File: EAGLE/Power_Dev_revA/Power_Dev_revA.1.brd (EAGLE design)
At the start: 63.5 x 31.8 mm, 36 parts, among them J5 MICRO_USB_SMD, Q1 SI2301CDS-T1-GE3, Q2 SI2301CDS-T1-GE3, U1 CN3791, U3 DW01A-G, U4 FS8205A

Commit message: Power PCB
added mounting holes
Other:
- board size 63.5 x 31.8 mm -> 63.5 x 38.1 mm
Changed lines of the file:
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@@
 <setting verticaltext="up"/>
 </settings>
-<grid distance="0.125" unitdist="inch" unit="inch" style="lines" multiple="1" display="no" altdistance="5" altunitdist="mil" altunit="mil"/>
+<grid distance="0.25" unitdist="inch" unit="inch" style="lines" multiple="1" display="no" altdistance="5" altunitdist="mil" altunit="mil"/>
 <layers>
 <layer number="1" name="Top" color="4" fill="1" visible="yes" active="yes"/>
@@
 <layer number="43" name="vRestrict" color="2" fill="10" visible="yes" active="yes"/>
 <layer number="44" name="Drills" color="7" fill="1" visible="no" active="yes"/>
-<layer number="45" name="Holes" color="7" fill="1" visible="no" active="yes"/>
+<layer number="45" name="Holes" color="7" fill="1" visible="yes" active="yes"/>
 <layer number="46" name="Milling" color="3" fill="1" visible="no" active="yes"/>
 <layer number="47" name="Measures" color="7" fill="1" visible="no" active="yes"/>
@@
 <plain>
 <wire x1="0" y1="0" x2="63.5" y2="0" width="0" layer="20"/>
-<wire x1="63.5" y1="0" x2="63.5" y2="31.75" width="0" layer="20"/>
-<wire x1="63.5" y1="31.75" x2="0" y2="31.75" width="0" layer="20"/>
-<wire x1="0" y1="31.75" x2="0" y2="0" width="0" layer="20"/>
+<wire x1="63.5" y1="0" x2="63.5" y2="38.1" width="0" layer="20"/>
+<wire x1="63.5" y1="38.1" x2="0" y2="38.1" width="0" layer="20"/>
+<wire x1="0" y1="38.1" x2="0" y2="0" width="0" layer="20"/>
 <text x="44.45" y="2.54" size="1.27" layer="21" font="vector" align="center">+</text>
 <text x="26.67" y="2.54" size="1.27" layer="21" font="vector" align="center">+</text>
@@
 <text x="8.89" y="2.54" size="1.27" layer="21" font="vector" align="center">C</text>
 <text x="1.27" y="2.54" size="1.27" layer="21" font="vector" align="center">D</text>
-<text x="31.75" y="15.875" size="2.54" layer="22" font="vector" rot="MR0" align="center">NSE LABS</text>
+<text x="31.75" y="34.29" size="1.524" layer="21" font="vector" align="center">NSE LABS</text>
+<hole x="12.7" y="34.29" drill="3.4"/>
+<hole x="50.8" y="34.29" drill="3.4"/>
 </plain>
 <attributes>
@@
 <vertex x="0" y="0"/>
 <vertex x="63.5" y="0"/>
-<vertex x="63.5" y="31.75"/>
-<vertex x="0" y="31.75"/>
+<vertex x="63.5" y="38.1"/>
+<vertex x="0" y="38.1"/>
 </polygon>
 <polygon width="0.254" layer="16" isolate="0.254">
 <vertex x="0" y="0"/>
-<vertex x="0" y="31.75"/>
-<vertex x="63.5" y="31.75"/>
+<vertex x="0" y="38.1"/>
+<vertex x="63.5" y="38.1"/>
 <vertex x="63.5" y="0"/>
 </polygon>

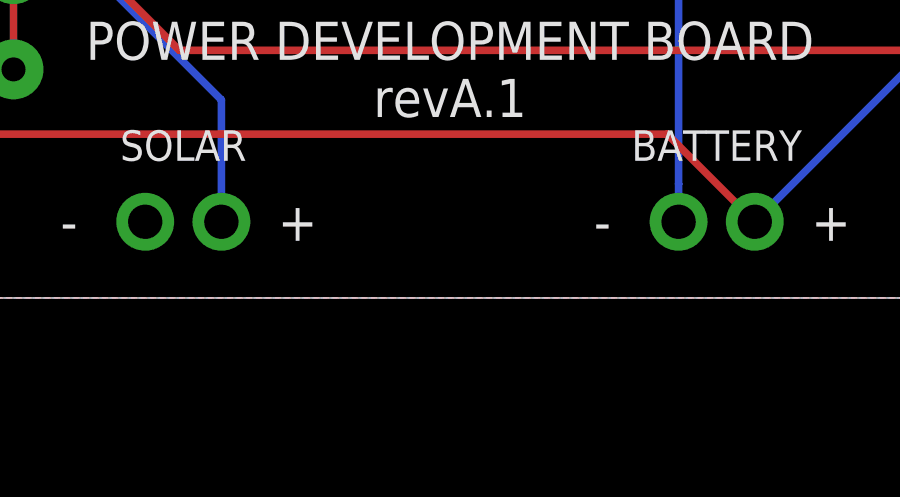
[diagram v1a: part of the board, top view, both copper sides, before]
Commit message: Power A.2
Added connector for battery
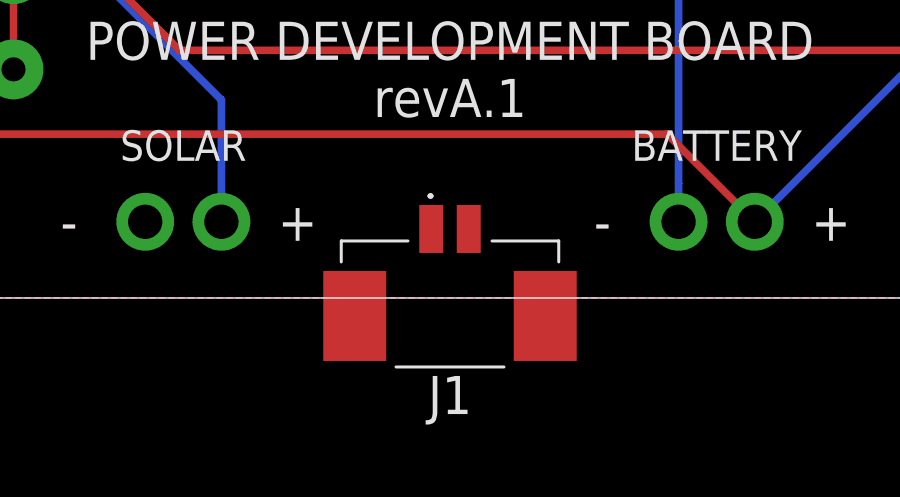
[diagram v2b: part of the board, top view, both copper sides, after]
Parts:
- added J1: 53261-0271, NSE LABS:532610271
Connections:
- net N$18: now also J1.2
- net N$20: now also J1.1
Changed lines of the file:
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@@
 <attribute name="NAME" x="58.42" y="5.08" size="1.016" layer="21" font="vector" rot="R180" align="center"/>
+</element>
+<element name="J1" library="NSE LABS" package="532610271" value="53261-0271" x="31.75" y="0" rot="R180">
+<attribute name="ARROW_PART_NUMBER" value="53261-0271" x="31.75" y="0" size="1.778" layer="27" rot="R180" display="off"/>
+<attribute name="ARROW_PRICE-STOCK" value="https://www.arrow.com/en/products/53261-0271/molex?region=nac" x="31.75" y="0" size="1.778" layer="27" rot="R180" display="off"/>
+<attribute name="DESCRIPTION" value="1.25mm Pitch, PicoBlade PCB Header, Single Row, Right-Angle, Surface Mount, Tin (Sn) Plating, Friction Lock,  Circuits, Tape and Reel" x="31.75" y="0" size="1.778" layer="27" rot="R180" display="off"/>
+<attribute name="HEIGHT" value="3.65mm" x="31.75" y="0" size="1.778" layer="27" rot="R180" display="off"/>
+<attribute name="MANUFACTURER_NAME" value="Molex" x="31.75" y="0" size="1.778" layer="27" rot="R180" display="off"/>
+<attribute name="MANUFACTURER_PART_NUMBER" value="53261-0271" x="31.75" y="0" size="1.778" layer="27" rot="R180" display="off"/>
+<attribute name="MOUSER_PART_NUMBER" value="538-53261-0271" x="31.75" y="0" size="1.778" layer="27" rot="R180" display="off"/>
+<attribute name="MOUSER_PRICE-STOCK" value="https://www.mouser.co.uk/ProductDetail/Molex/53261-0271?qs=%252B72YyncTwW%252B8%252BBjraxGf3A%3D%3D" x="31.75" y="0" size="1.778" layer="27" rot="R180" display="off"/>
 </element>
 </elements>
@@
 <via x="49.53" y="27.559" extent="1-16" drill="0.35"/>
 <wire x1="39.37" y1="2.54" x2="39.37" y2="3.81" width="0.254" layer="16"/>
+<contactref element="J1" pad="2"/>
+<wire x1="32.375" y1="2.3" x2="39.37" y2="2.54" width="0" layer="19" extent="1-1"/>
 </signal>
 <signal name="N$19">
@@
 <wire x1="13.716" y1="7.747" x2="13.716" y2="13.843" width="0.254" layer="1"/>
 <wire x1="13.716" y1="13.843" x2="14.748" y2="14.875" width="0.254" layer="1"/>
+<contactref element="J1" pad="1"/>
+<wire x1="31.125" y1="2.3" x2="16.002" y2="5.461" width="0" layer="19" extent="1-1"/>
 </signal>
 <signal name="N$6">
